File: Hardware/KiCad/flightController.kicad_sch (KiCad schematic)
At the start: 0 parts

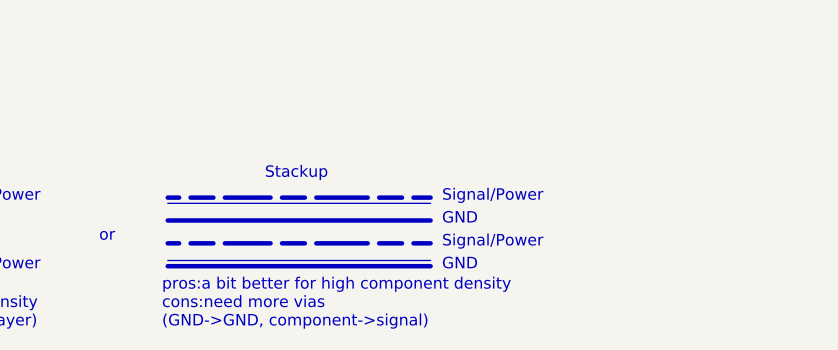
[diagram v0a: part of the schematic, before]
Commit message: added the bmp388 pressure sensor
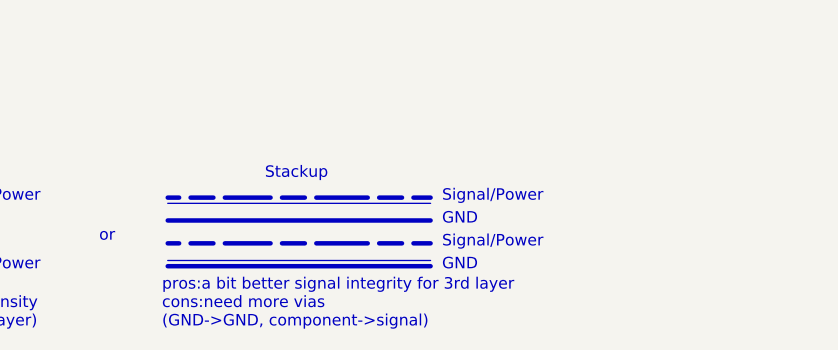
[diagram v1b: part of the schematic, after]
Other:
- note added: "pros:a bit better signal integrity for 3rd layer cons:need more vias (GND->GND, component->signal)"
- note removed: "pros:a bit better for high component density cons:need more vias (GND->GND, component->signal)"
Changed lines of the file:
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@@
     (effects (font (size 1.27 1.27)) (justify left bottom))
   )
-  (text "pros:a bit better for high component density\ncons:need more vias \n(GND->GND, component->signal)"
+  (text "pros:a bit better signal integrity for 3rd layer\ncons:need more vias \n(GND->GND, component->signal)"
     (at 117.475 189.865 0)
     (effects (font (size 1.27 1.27)) (justify left bottom))
@@
       (reference "#PWR?") (unit 1) (value "GND") (footprint "")
     )
+    (path "/c06e5e7c-c9d3-4ec8-9cbe-adebe02c2230/50241047-caa4-455c-a942-a06592e82f76"
+      (reference "#PWR?") (unit 1) (value "+3.3V") (footprint "")
+    )
+    (path "/c06e5e7c-c9d3-4ec8-9cbe-adebe02c2230/51c3c109-6623-4c33-982b-1f2e6bc2df2f"
+      (reference "#PWR?") (unit 1) (value "GND") (footprint "")
+    )
     (path "/c06e5e7c-c9d3-4ec8-9cbe-adebe02c2230/53384804-c5e4-4e5a-b16e-3d0407e5d2ac"
       (reference "#PWR?") (unit 1) (value "GND") (footprint "")
     )
-    (path "/c06e5e7c-c9d3-4ec8-9cbe-adebe02c2230/548e3652-a56e-4bba-8696-8149756d1f0d"
+    (path "/c06e5e7c-c9d3-4ec8-9cbe-adebe02c2230/55082cc1-c956-45a6-b2b5-3db02a6da9d0"
       (reference "#PWR?") (unit 1) (value "GND") (footprint "")
     )
@@
       (reference "#PWR?") (unit 1) (value "GND") (footprint "")
     )
-    (path "/c06e5e7c-c9d3-4ec8-9cbe-adebe02c2230/5dec71ad-9fc4-4863-be4e-09ade2f95c6e"
-      (reference "#PWR?") (unit 1) (value "GND") (footprint "")
-    )
     (path "/c06e5e7c-c9d3-4ec8-9cbe-adebe02c2230/67f216cd-7460-434d-bca3-2f9633ea8009"
-      (reference "#PWR?") (unit 1) (value "GND") (footprint "")
-    )
-    (path "/c06e5e7c-c9d3-4ec8-9cbe-adebe02c2230/687e3777-603d-481c-8889-96820b124f35"
       (reference "#PWR?") (unit 1) (value "GND") (footprint "")
     )
@@
       (reference "#PWR?") (unit 1) (value "GND") (footprint "")
     )
-    (path "/c06e5e7c-c9d3-4ec8-9cbe-adebe02c2230/87a66370-3d8e-48b9-936f-838ac4e24e98"
-      (reference "#PWR?") (unit 1) (value "+3.3V") (footprint "")
-    )
     (path "/b07d43c0-4d18-408b-9d9e-0ce113f0ef7f/89500d01-f58d-4b3d-bfa3-554e0b5f015e"
       (reference "#PWR?") (unit 1) (value "+3.3V") (footprint "")
@@
       (reference "#PWR?") (unit 1) (value "GND") (footprint "")
     )
-    (path "/c06e5e7c-c9d3-4ec8-9cbe-adebe02c2230/9a8915ab-d215-4c18-a347-e21a73cf89b5"
-      (reference "#PWR?") (unit 1) (value "GND") (footprint "")
-    )
     (path "/c06e5e7c-c9d3-4ec8-9cbe-adebe02c2230/a05ee653-d845-4689-8ea6-4492527dea39"
       (reference "#PWR?") (unit 1) (value "GND") (footprint "")
@@
     (path "/c06e5e7c-c9d3-4ec8-9cbe-adebe02c2230/a8c4a82b-225b-4372-8af5-aa6a9bac1820"
       (reference "#PWR?") (unit 1) (value "+3.3V") (footprint "")
+    )
+    (path "/c06e5e7c-c9d3-4ec8-9cbe-adebe02c2230/a90648b1-b377-46ef-8d40-33f7fb6bca6a"
+      (reference "#PWR?") (unit 1) (value "GND") (footprint "")
     )
     (path "/c06e5e7c-c9d3-4ec8-9cbe-adebe02c2230/aa889b6e-af64-47ad-83e7-ab2839f0288c"
@@
       (reference "#PWR?") (unit 1) (value "VCC") (footprint "")
     )
-    (path "/c06e5e7c-c9d3-4ec8-9cbe-adebe02c2230/d8037e40-9a52-43a0-84bc-dbc598e06ca2"
-      (reference "#PWR?") (unit 1) (value "GND") (footprint "")
-    )
-    (path "/c06e5e7c-c9d3-4ec8-9cbe-adebe02c2230/dda22a01-75a2-457f-926d-a704e3bcc43c"
-      (reference "#PWR?") (unit 1) (value "GND") (footprint "")
+    (path "/c06e5e7c-c9d3-4ec8-9cbe-adebe02c2230/d8dbc099-3999-474e-bc20-5aa4b41f9e9b"
+      (reference "#PWR?") (unit 1) (value "+3.3V") (footprint "")
     )
     (path "/b07d43c0-4d18-408b-9d9e-0ce113f0ef7f/ddc588d3-e808-4d46-bdf2-3c6ff800a1b0"
@@
       (reference "#PWR?") (unit 1) (value "+5V") (footprint "")
     )
-    (path "/c06e5e7c-c9d3-4ec8-9cbe-adebe02c2230/0214a11f-0118-4fa9-9cf3-e31efcf7729b"
-      (reference "C?") (unit 1) (value "10n") (footprint "")
-    )
     (path "/36610400-2025-4f94-8ad5-a4c55b7ca6d5/0607f369-478b-4c39-ac7e-788d6cad2c8a"
       (reference "C?") (unit 1) (value "100n") (footprint "")
@@
       (reference "C?") (unit 1) (value "2u2") (footprint "")
     )
+    (path "/c06e5e7c-c9d3-4ec8-9cbe-adebe02c2230/50ef776e-1890-489b-b3a9-2368d96f2098"
+      (reference "C?") (unit 1) (value "100n") (footprint "")
+    )
     (path "/c06e5e7c-c9d3-4ec8-9cbe-adebe02c2230/6410dc00-410e-4943-9184-22ccd356c3b6"
       (reference "C?") (unit 1) (value "220n") (footprint "")
@@
       (reference "C?") (unit 1) (value "100n") (footprint "")
     )
-    (path "/c06e5e7c-c9d3-4ec8-9cbe-adebe02c2230/99c8ced5-ab29-4161-bf4d-ea6944471e16"
-      (reference "C?") (unit 1) (value "10u") (footprint "")
-    )
-    (path "/c06e5e7c-c9d3-4ec8-9cbe-adebe02c2230/9d35f413-a493-481a-a049-98566c301aa7"
-      (reference "C?") (unit 1) (value "100n") (footprint "")
-    )
     (path "/b07d43c0-4d18-408b-9d9e-0ce113f0ef7f/9db13b45-0dac-488d-80cf-83c4a45aa607"
       (reference "C?") (unit 1) (value "100n") (footprint "")
@@
       (reference "C?") (unit 1) (value "100n") (footprint "")
     )
+    (path "/b07d43c0-4d18-408b-9d9e-0ce113f0ef7f/ba93e0ca-be08-4f2a-ac13-94d4bf3448d1"
+      (reference "C?") (unit 1) (value "100n") (footprint "")
+    )
     (path "/36610400-2025-4f94-8ad5-a4c55b7ca6d5/bac6658c-b7ad-4c4b-8b13-edb4ebecc418"
       (reference "C?") (unit 1) (value "10u") (footprint "")
@@
       (reference "C?") (unit 1) (value "100n") (footprint "")
     )
-    (path "/b07d43c0-4d18-408b-9d9e-0ce113f0ef7f/c7782017-c062-488e-88e2-65633a7659f9"
-      (reference "C?") (unit 1) (value "500n") (footprint "")
-    )
     (path "/36610400-2025-4f94-8ad5-a4c55b7ca6d5/c7d7f1cf-73a0-4de6-9ca3-c383fe1ebf6c"
       (reference "C?") (unit 1) (value "12p") (footprint "")
     )
-    (path "/b07d43c0-4d18-408b-9d9e-0ce113f0ef7f/dcf8e2c8-6076-4f37-bf5c-1157a4ac3060"
-      (reference "C?") (unit 1) (value "500n") (footprint "")
-    )
     (path "/36610400-2025-4f94-8ad5-a4c55b7ca6d5/ddc1df03-ee8e-42d7-8bbb-107eeba466a3"
       (reference "C?") (unit 1) (value "100n") (footprint "")
@@
       (reference "C?") (unit 1) (value "10n") (footprint "")
     )
+    (path "/b07d43c0-4d18-408b-9d9e-0ce113f0ef7f/e373ab6f-8d8d-4a47-bf0c-630049f68d5d"
+      (reference "C?") (unit 1) (value "100n") (footprint "")
+    )
     (path "/36610400-2025-4f94-8ad5-a4c55b7ca6d5/e5494ac5-762d-4d49-99c7-3d354909a81a"
       (reference "C?") (unit 1) (value "2u2") (footprint "")
     )
-    (path "/c06e5e7c-c9d3-4ec8-9cbe-adebe02c2230/eb3b99e2-5aa9-4fa7-bce5-e207cf87bc70"
-      (reference "C?") (unit 1) (value "4u7") (footprint "")
-    )
     (path "/36610400-2025-4f94-8ad5-a4c55b7ca6d5/ee3dd1d0-7e92-404f-b416-8e6ac2c6488f"
       (reference "C?") (unit 1) (value "10u") (footprint "")
@@
       (reference "FB?") (unit 1) (value "100@100MHz") (footprint "")
     )
-    (path "/c06e5e7c-c9d3-4ec8-9cbe-adebe02c2230/b04d7f80-f987-48f1-85a2-2e55f687be42"
-      (reference "FB?") (unit 1) (value "100@100MHz") (footprint "")
-    )
     (path "/36610400-2025-4f94-8ad5-a4c55b7ca6d5/e4447019-cc1b-46a3-925a-8d87bf9cc7bc"
       (reference "FB?") (unit 1) (value "100@100MHz") (footprint "")
@@
       (reference "U?") (unit 1) (value "SMF05CT1G") (footprint "Package_TO_SOT_SMD:SOT-363_SC-70-6")
     )
-    (path "/c06e5e7c-c9d3-4ec8-9cbe-adebe02c2230/6fdaeed4-3239-4d17-86f0-69239ae20ade"
-      (reference "U?") (unit 1) (value "ICM-20689") (footprint "Sensor_Motion:InvenSense_QFN-24_4x4mm_P0.5mm")
-    )
     (path "/b07d43c0-4d18-408b-9d9e-0ce113f0ef7f/772ad8f2-b74b-4273-8061-61524384334f"
       (reference "U?") (unit 1) (value "SMF05CT1G") (footprint "Package_TO_SOT_SMD:SOT-363_SC-70-6")
@@
       (reference "U?") (unit 1) (value "SMF05CT1G") (footprint "Package_TO_SOT_SMD:SOT-363_SC-70-6")
     )
+    (path "/c06e5e7c-c9d3-4ec8-9cbe-adebe02c2230/910688d1-5450-4807-98b4-1e8f4ed3e180"
+      (reference "U?") (unit 1) (value "BMP388") (footprint "PQFN50P200X200X80-10N")
+    )
     (path "/b07d43c0-4d18-408b-9d9e-0ce113f0ef7f/96d03dac-f299-4cb5-9afa-18d3ec0f3b01"

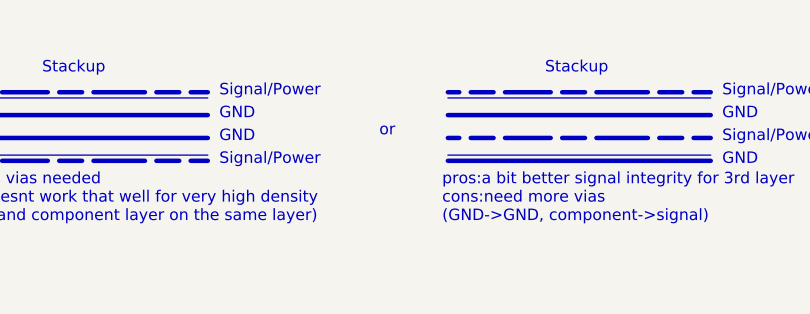
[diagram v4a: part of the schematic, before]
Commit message: Added pinlables, added SD cardholder footprint, fixed VBUS connection, added termination resistors for high frequency signals, improved schematic layout
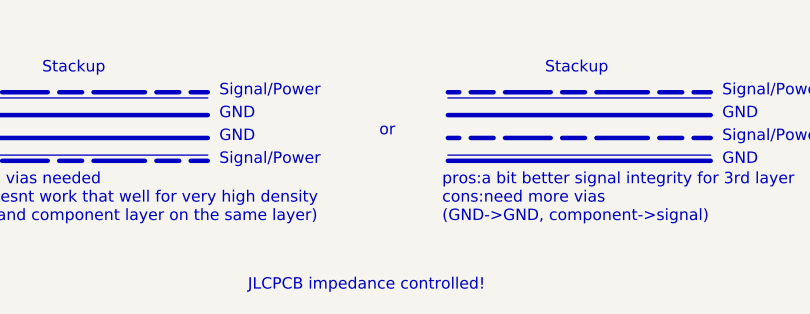
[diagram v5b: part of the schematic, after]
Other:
- note added: "JLCPCB impedance controlled!"
